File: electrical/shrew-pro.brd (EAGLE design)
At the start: 18 x 27 mm, 55 parts, among them IC1 LMR16006YQ3DDCTQ1, U1 ESP32-PICO-D4, U2 SX1280IMLTRT, U3 DRV8244HQRYJRQ1, U4 DRV8244HQRYJRQ1, X1 PIN-1X-BIG, X2 PIN-1X-BIG, X3 PIN-1X-BIG, X4 PIN-1X-BIG, X5 PIN-1X-BIG, X6 PIN-1X-BIG, Y1 2450FM07D0034T, Y2 52MHz TCXO

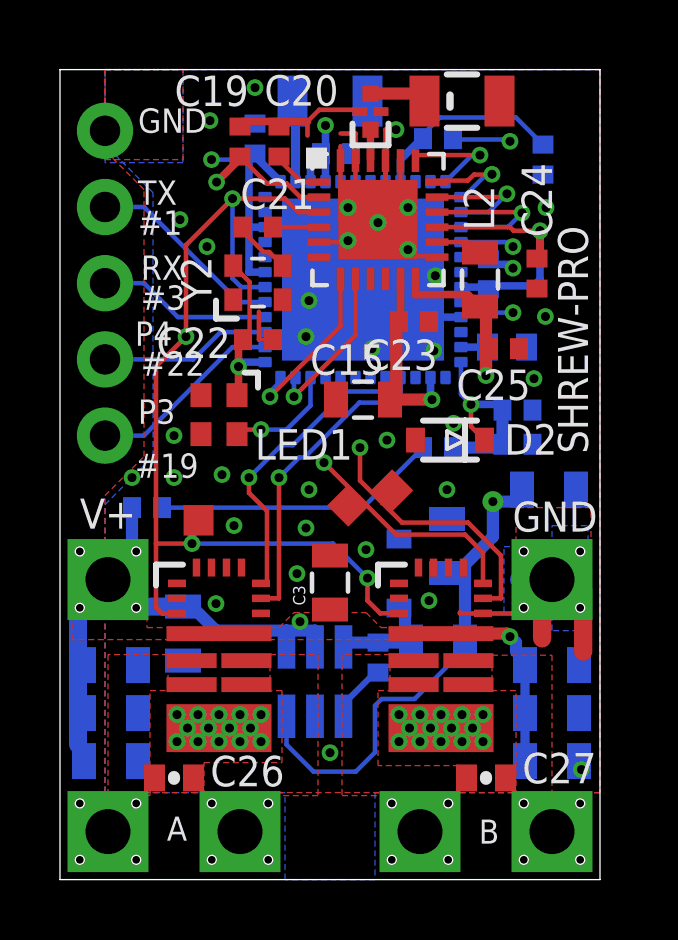
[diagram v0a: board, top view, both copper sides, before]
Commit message: shrew-pro with additional capacitors
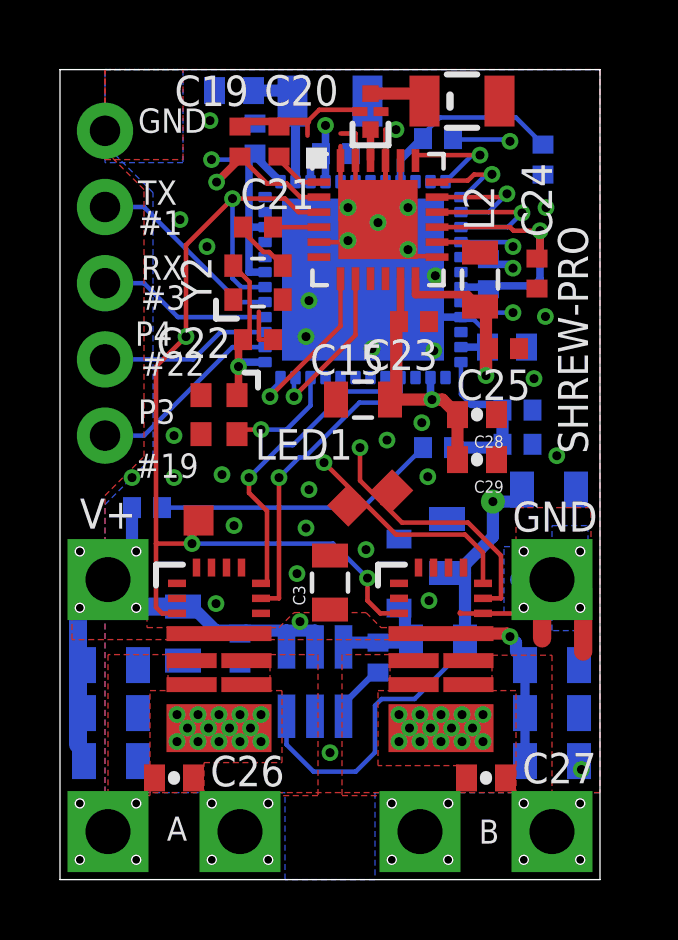
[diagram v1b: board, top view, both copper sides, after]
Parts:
- removed D2: 3V6, shrew-common:SOD-323
- added C28, C29: 100nF, shrew-common:0402-CAP
- added C30: 100nF, shrew-common:0402-REV
- added C31: 0.5pF, shrew-common:0402-CAP
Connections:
- net +24V: now also C30.2
- net 3.3V: now also C28.2, C29.2
- net BATT-ADC: no longer D2.1
- net GND: now also C28.1, C29.1, C30.1, C31.2; no longer D2.2
- net N$1: now also C31.1
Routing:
- net 3.3V: track 51.5 -> 54.1 mm
- net GND: track 50.3 -> 48.4 mm
- net N$1: track 2.78 -> 4.43 mm
- net BATT-ADC: track 6.98 -> 5.60 mm, vias 1 -> 0
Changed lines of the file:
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@@
 <layers>
 <layer number="1" name="Top" color="4" fill="1" visible="yes" active="yes"/>
-<layer number="2" name="Route2" color="1" fill="3" visible="no" active="yes"/>
+<layer number="2" name="Route2" color="1" fill="3" visible="yes" active="yes"/>
 <layer number="3" name="Route3" color="4" fill="3" visible="no" active="no"/>
 <layer number="4" name="Route4" color="1" fill="4" visible="no" active="no"/>
@@
 <layer number="13" name="Route13" color="4" fill="5" visible="no" active="no"/>
 <layer number="14" name="Route14" color="1" fill="6" visible="no" active="no"/>
-<layer number="15" name="Route15" color="4" fill="6" visible="no" active="yes"/>
+<layer number="15" name="Route15" color="4" fill="6" visible="yes" active="yes"/>
 <layer number="16" name="Bottom" color="1" fill="1" visible="yes" active="yes"/>
 <layer number="17" name="Pads" color="2" fill="1" visible="yes" active="yes"/>
@@
 <layer number="21" name="tPlace" color="7" fill="1" visible="yes" active="yes"/>
 <layer number="22" name="bPlace" color="7" fill="1" visible="yes" active="yes"/>
-<layer number="23" name="tOrigins" color="15" fill="1" visible="no" active="yes"/>
-<layer number="24" name="bOrigins" color="15" fill="1" visible="no" active="yes"/>
+<layer number="23" name="tOrigins" color="15" fill="1" visible="yes" active="yes"/>
+<layer number="24" name="bOrigins" color="15" fill="1" visible="yes" active="yes"/>
 <layer number="25" name="tNames" color="7" fill="1" visible="no" active="yes"/>
 <layer number="26" name="bNames" color="7" fill="1" visible="no" active="yes"/>
@@
 <layer number="40" name="bKeepout" color="1" fill="11" visible="no" active="yes"/>
 <layer number="41" name="tRestrict" color="4" fill="10" visible="no" active="yes"/>
-<layer number="42" name="bRestrict" color="1" fill="10" visible="no" active="yes"/>
+<layer number="42" name="bRestrict" color="1" fill="10" visible="yes" active="yes"/>
 <layer number="43" name="vRestrict" color="2" fill="10" visible="no" active="yes"/>
 <layer number="44" name="Drills" color="7" fill="1" visible="no" active="yes"/>
@@
 <dimension x1="1.6" y1="1.6" x2="6" y2="1.6" x3="3.8" y3="-1.7" textsize="0.8128" textratio="6" layer="216" dtype="horizontal" width="0.08"/>
 <dimension x1="1.5" y1="14.8" x2="0" y2="15.6" x3="0.75" y3="16.1" textsize="0.8128" textratio="6" layer="216" dtype="horizontal" width="0.08"/>
+<wire x1="1.93" y1="13.02" x2="1.93" y2="12.79" width="0" layer="42"/>
 </plain>
 <attributes>
@@
 <attribute name="NAME" x="6.5" y="14" size="1.016" layer="25" font="vector"/>
 </element>
-<element name="D2" library="shrew-common" package="SOD-323" value="3V6" x="13" y="14.65" smashed="yes" rot="R180">
-<attribute name="NAME" x="14.811" y="14.166" size="1.016" layer="25" font="vector"/>
-</element>
 <element name="R4" library="shrew-common" package="0402-REV" value="10K" x="15.25" y="14.51" smashed="yes" rot="MR0">
 <attribute name="NAME" x="16.139" y="15.2085" size="0.4064" layer="26" rot="MR0"/>
@@
 <element name="TP2" library="shrew-common" package="1X01-1.0MM-TP" value="" x="9.612134375" y="12.4707125" rot="R45"/>
 <element name="TP3" library="shrew-common" package="1X01-1.0MM-TP" value="" x="4.62" y="11.97"/>
+<element name="C31" library="shrew-common" package="0402-CAP" value="0.5pF" x="5.8" y="26.3" rot="MR0"/>
+<element name="C28" library="shrew-common" package="0402-CAP" value="100nF" x="13.9" y="15.5" rot="R180"/>
+<element name="C29" library="shrew-common" package="0402-CAP" value="100nF" x="13.9" y="14" rot="R180"/>
+<element name="C30" library="shrew-common" package="0402-REV" value="100nF" x="6" y="7.7" rot="MR90"/>
 </elements>
 <signals>
@@
 <wire x1="9.35" y1="22" x2="10.6" y2="22" width="0.1524" layer="1"/>
 <contactref element="LED1" pad="3"/>
-<contactref element="D2" pad="2"/>
 <contactref element="R4" pad="1"/>
 <contactref element="C18" pad="2"/>
@@
 <via x="4.9" y="21.1" extent="1-16" drill="0.3" shape="octagon"/>
 <via x="5" y="25.3" extent="1-16" drill="0.3" shape="octagon"/>
-<via x="6.5" y="26.4" extent="1-16" drill="0.3" shape="octagon"/>
 <via x="16.2" y="22.4" extent="1-16" drill="0.3" shape="octagon"/>
 <via x="15.8" y="16.7" extent="1-16" drill="0.3" shape="octagon"/>
@@
 <wire x1="10.85" y1="22.4" x2="11.6" y2="22.4" width="0.1524" layer="1"/>
 <wire x1="7.3" y1="25.1" x2="7.3" y2="25.27" width="0.254" layer="1"/>
-<via x="13.12" y="15.21" extent="1-16" drill="0.3" shape="octagon"/>
 <via x="15.1" y="20.38" extent="1-16" drill="0.3" shape="octagon"/>
 <wire x1="14.28" y1="20.68" x2="14.45" y2="20.51" width="0.254" layer="16"/>
 <wire x1="14.45" y1="20.51" x2="15.1" y2="20.51" width="0.254" layer="16"/>
 <wire x1="15.1" y1="20.51" x2="15.1" y2="20.38" width="0.254" layer="16"/>
-<wire x1="12.46" y1="17.62" x2="13.12" y2="16.96" width="0.1524" layer="15"/>
-<wire x1="13.12" y1="16.96" x2="13.12" y2="15.21" width="0.1524" layer="15"/>
 <wire x1="10.9" y1="14.65" x2="10.9" y2="17.2" width="0.1524" layer="15"/>
 <wire x1="10.9" y1="17.2" x2="10.41" y2="17.69" width="0.1524" layer="15"/>
@@
 <contactref element="C4" pad="2"/>
 <contactref element="C2" pad="2"/>
-<via x="12.9" y="13" extent="1-16" drill="0.3" shape="octagon"/>
 <via x="5.8" y="11.8" extent="1-16" drill="0.3" shape="octagon"/>
 <via x="8.2" y="11.72" extent="1-16" drill="0.3" shape="octagon"/>
@@
 <wire x1="14.3" y1="25.4" x2="15.3" y2="25.4" width="0.3048" layer="2"/>
 <wire x1="15.3" y1="25.4" x2="15.9" y2="24.8" width="0.3048" layer="2"/>
+<contactref element="C31" pad="2"/>
+<contactref element="C28" pad="1"/>
+<contactref element="C29" pad="1"/>
+<via x="12.26" y="13.43" extent="1-16" drill="0.3" shape="octagon"/>
+<via x="12.06" y="15.23" extent="1-16" drill="0.3" shape="octagon"/>
+<via x="16.56" y="14.13" extent="1-16" drill="0.3" shape="octagon"/>
+<wire x1="13.33" y1="18.66" x2="13.8" y2="18.66" width="0.1524" layer="16"/>
+<wire x1="13.8" y1="18.66" x2="14.02" y2="18.44" width="0.1524" layer="16"/>
+<contactref element="C30" pad="1"/>
 </signal>
 <signal name="VDD_SDIO">
@@
 <wire x1="11.82" y1="6.02" x2="13.5" y2="7.7" width="0.1524" layer="16"/>
 <wire x1="13.5" y1="7.7" x2="13.5" y2="7.9" width="0.1524" layer="16"/>
-<via x="14.43" y="12.6" extent="1-16" drill="0.3" diameter="0.7" shape="octagon" alwaysstop="yes"/>
+<via x="14.43" y="12.6" extent="1-16" drill="0.3" diameter="0.8" shape="octagon" alwaysstop="yes"/>
 <contactref element="C4" pad="1"/>
 <contactref element="C2" pad="1"/>
@@
 <wire x1="14.43" y1="12.6" x2="15.4" y2="12.6" width="0.4064" layer="16"/>
 <wire x1="15.4" y1="12.6" x2="15.4" y2="13" width="0.4064" layer="16"/>
+<contactref element="C28" pad="2"/>
+<contactref element="C29" pad="2"/>
+<wire x1="12.4" y1="16" x2="12.75" y2="16" width="0.4064" layer="1"/>
+<wire x1="12.75" y1="16" x2="13.25" y2="15.5" width="0.4064" layer="1"/>
+<wire x1="13.25" y1="15.5" x2="13.25" y2="14" width="0.4064" layer="1"/>
 </signal>
 <signal name="U0TXD">
@@
 <wire x1="7.85" y1="23.265" x2="7.85" y2="25.95" width="0.3048" layer="16"/>
 <wire x1="7.85" y1="25.95" x2="7.75" y2="25.95" width="0.3048" layer="16"/>
+<contactref element="C31" pad="1"/>
+<wire x1="6.45" y1="26.3" x2="7.75" y2="26.3" width="0.4064" layer="16"/>
+<wire x1="7.75" y1="26.3" x2="7.75" y2="25.95" width="0.4064" layer="16"/>
 </signal>
 <signal name="N$6">
@@
 <contactref element="R3" pad="1"/>
 <contactref element="R4" pad="2"/>
-<contactref element="D2" pad="1"/>
 <contactref element="C18" pad="1"/>
 <contactref element="U1" pad="24"/>
-<via x="13.7" y="15.84" extent="1-16" drill="0.3" shape="octagon"/>
 <wire x1="14.75" y1="14.51" x2="14.75" y2="15.65" width="0.4064" layer="16"/>
 <wire x1="13.1" y1="14.4" x2="14.5" y2="14.4" width="0.4064" layer="16"/>
@@
 <wire x1="13.7" y1="15.84" x2="13.365" y2="16.175" width="0.1524" layer="16"/>
 <wire x1="13.365" y1="16.175" x2="13.365" y2="17.25" width="0.1524" layer="16"/>
-<wire x1="14.15" y1="14.65" x2="13.7" y2="15.1" width="0.1524" layer="1"/>
-<wire x1="13.7" y1="15.1" x2="13.7" y2="15.84" width="0.1524" layer="1"/>
 <wire x1="13.7" y1="15.84" x2="14.75" y2="15.84" width="0.254" layer="16"/>
 <wire x1="14.75" y1="15.84" x2="14.75" y2="15.65" width="0.254" layer="16"/>
@@
 <wire x1="8.5" y1="7.755" x2="8.5" y2="8.3" width="0.4064" layer="16"/>
 <wire x1="8.5" y1="8.3" x2="7.55" y2="8.3" width="0.4064" layer="16"/>
-<wire x1="7.55" y1="8.3" x2="5.2" y2="8.3" width="0.4064" layer="16"/>
+<wire x1="7.55" y1="8.3" x2="6.2" y2="8.3" width="0.4064" layer="16"/>
+<wire x1="6.2" y1="8.3" x2="5.2" y2="8.3" width="0.4064" layer="16"/>
 <wire x1="5.2" y1="8.3" x2="4.4" y2="9.1" width="0.4064" layer="16"/>
 <wire x1="4.4" y1="9.1" x2="4.1" y2="9.1" width="0.4064" layer="16"/>
@@
 <vertex x="0.5" y="7.7"/>
 </polygon>
+<contactref element="C30" pad="2"/>
+<wire x1="6" y1="8.2" x2="6.2" y2="8.3" width="0.1524" layer="16"/>
 </signal>
 <signal name="MOTOR2">

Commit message: PCB changes for better EMI emissions
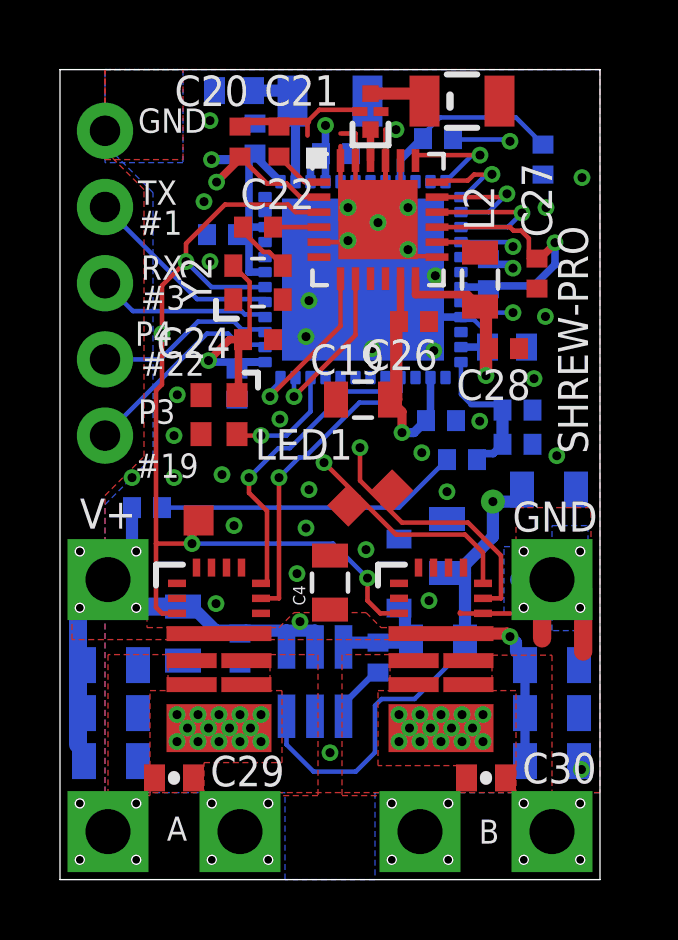
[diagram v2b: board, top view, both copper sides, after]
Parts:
- added C32: DNP, shrew-common:0402-CAP
- ANT1, ANT2: value 74889302450 -> ANT3216LL00R2400A
- C12: value 100n -> 10u; device shrew-common:0402-REV -> shrew-common:0805
- C15: value 10uF 25V -> 100n; device shrew-common:0805 -> shrew-common:0402-REV
- C16, C18: value 470n -> 100n
- C17: value DNP -> 100n; device shrew-common:0402-CAP -> shrew-common:0402-REV
- C19: value 10n -> 10uF 25V; device shrew-common:0402-REV -> shrew-common:0805
- C21: value 1n -> 10n
- C22: value 100n -> 1n
- C23: value 100n -> 470n
- C25: value 470n -> 0.5pF; device shrew-common:0402-REV -> shrew-common:0402-CAP
- C26, C27: device shrew-common:0402-CAP -> shrew-common:0402-REV
- C28: value 100nF -> 470n; device shrew-common:0402-CAP -> shrew-common:0402-REV
- C29: value 100nF -> 100n
- C3: value 10u -> 100n; device shrew-common:0805 -> shrew-common:0402-REV
- C30: value 100nF -> 100n; device shrew-common:0402-REV -> shrew-common:0402-CAP
- C31: value 0.5pF -> 470n; device shrew-common:0402-CAP -> shrew-common:0402-REV
- U1: value ESP32-PICO-D4 -> SX1280IMLTRT; device shrew-core:PQFN50P700X700X104-49N -> shrew-core:QFN24_4X4_SEM
- U2: value SX1280IMLTRT -> ESP32-PICO-D4; device shrew-core:QFN24_4X4_SEM -> shrew-core:PQFN50P700X700X104-49N
- moved C12 23.0 mm to (16.4, 3.95), turned to 180 degrees
- moved C26 17.2 mm to (11.8, 18.6)
- moved C5 17.2 mm to (16.3, 13.0)
- moved C27 16.9 mm to (15.9, 20.2), turned to 90 degrees
- moved C29 14.6 mm to (3.80, 3.39)
- moved C31 14.2 mm to (15.2, 15.7), turned to 180 degrees
- moved C25 12.4 mm to (5.80, 26.3), flipped to the bottom, turned to 0 degrees
- moved C9 12.3 mm to (4.10, 8.20), turned to 270 degrees
- moved C16 9.63 mm to (6.50, 24.7)
- moved C13 9.56 mm to (12.7, 15.3), turned to 0 degrees
- moved C24 9.56 mm to (6.60, 18.0), turned to 180 degrees
- moved C19 9.53 mm to (10.1, 16.0), turned to 180 degrees
- moved C30 9.26 mm to (14.2, 3.39), flipped to the top, turned to 180 degrees
- moved C14 9.15 mm to (5.90, 16.5)
- moved C17 8.61 mm to (9.20, 24.2), turned to 180 degrees
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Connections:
- net +24V: now also C12.1, C3.2, C4.1; no longer C3.1, C30.2, C5.1
- net 3.3V: now also C13.2, C14.2, C15.2, C16.1, C17.1, C18.1, C19.1, C26.2, C27.2, C5.1, U1.11, U1.15, U2.1, U2.19, U2.26, U2.3, U2.37, U2.4, U2.43, U2.46; no longer C12.1, C13.1, C14.1, C15.1, C22.2, C23.2, C28.2, C29.2, C4.1, U1.1, U1.19, U1.26, U1.3, U1.37, U1.4, U1.43, U1.46, U2.11, U2.15
- net AUX1: now also U2.38; no longer U1.38
- net AUX2: now also U2.39; no longer U1.39
- net BATT-ADC: now also C31.1, U2.24; no longer C18.1, U1.24
- net ESP-BOOT: now also C32.2, U2.23; no longer C17.2, U1.23
- net ESP-EN: now also C23.2, U2.9; no longer C16.2, U1.9
- net GND: now also C13.1, C14.1, C15.1, C16.2, C17.2, C19.2, C21.1, C25.2, C26.1, C27.1, C3.1, C32.1, U1.13, U1.20, U1.23, U1.24, U1.25, U1.5, U2.49; no longer C13.2, C14.2, C15.2, C16.1, C17.1, C19.1, C22.1, C25.1, C29.1, C3.2, C30.1, U1.49, U2.13, U2.20, U2.23, U2.24, U2.25, U2.5
- net MOTOR1: now also C29.1; no longer C26.1
- net MOTOR2: now also C29.2; no longer C26.2
- net MOTOR3: now also C30.1; no longer C27.1
- net MOTOR4: now also C30.2; no longer C27.2
- net N$1: now also C25.1, U2.2; no longer C31.1, U1.2
- net N$11: now also C21.2, U1.1; no longer C20.2, U2.1
- net N$2: now also C22.1; no longer C21.1
- net N$3: now also C22.2, U1.4; no longer C21.2, U2.4
- net N$5: now also U2.17; no longer U1.17
- net N$6: now also U1.22; no longer U2.22
- net N$8: now also U2.22; no longer U1.22
- net N$9: now also U1.14; no longer U2.14
- net RADIO-BUSY: now also U1.7, U2.36; no longer U1.36, U2.7
- net RADIO-CS: now also U1.19, U2.12; no longer U1.12, U2.19
- net RADIO-DIO: now also U1.8, U2.35; no longer U1.35, U2.8
- net RADIO-RST: now also U1.3, U2.42; no longer U1.42, U2.3
- net RADIO-VDD: now also C20.2, C28.2, U1.12, U1.2; no longer C19.2, C25.2, U2.12, U2.2
- net RGBLED: now also U2.34; no longer U1.34
- net SIG1: now also U2.20; no longer U1.20
- net SIG2: now also U2.16; no longer U1.16
- net SIG3: now also U2.28; no longer U1.28
- net SIG4: now also U2.29; no longer U1.29
- net SPI-MISO: now also U1.16, U2.15; no longer U1.15, U2.16
- net SPI-MOSI: now also U1.17, U2.14; no longer U1.14, U2.17
- net SPI-SCK: now also U1.18, U2.13; no longer U1.13, U2.18
- net U0RXD: now also U2.40; no longer U1.40
- net U0TXD: now also U2.41; no longer U1.41
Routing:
- net GND: track 48.4 -> 78.2 mm, vias 63 -> 66
- net 3.3V: track 54.1 -> 57.7 mm
- net RADIO-RST: track 32.8 -> 31.7 mm
- net V-ADC: track 9.53 -> 10.2 mm
- net BATT-ADC: track 5.60 -> 4.99 mm
